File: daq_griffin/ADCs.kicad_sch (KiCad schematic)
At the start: 12 parts, among them J13 SENSOR, U13 ADS8866

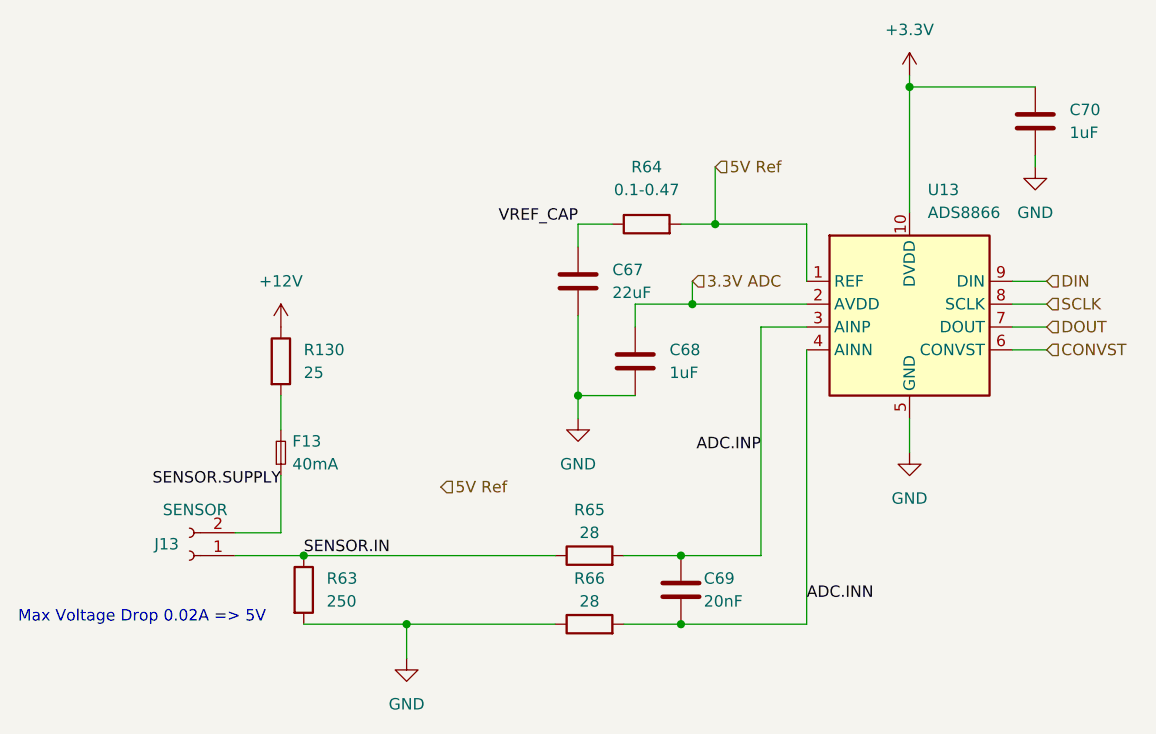
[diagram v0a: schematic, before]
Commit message: Add thermocouple connectors and minor layout changes.
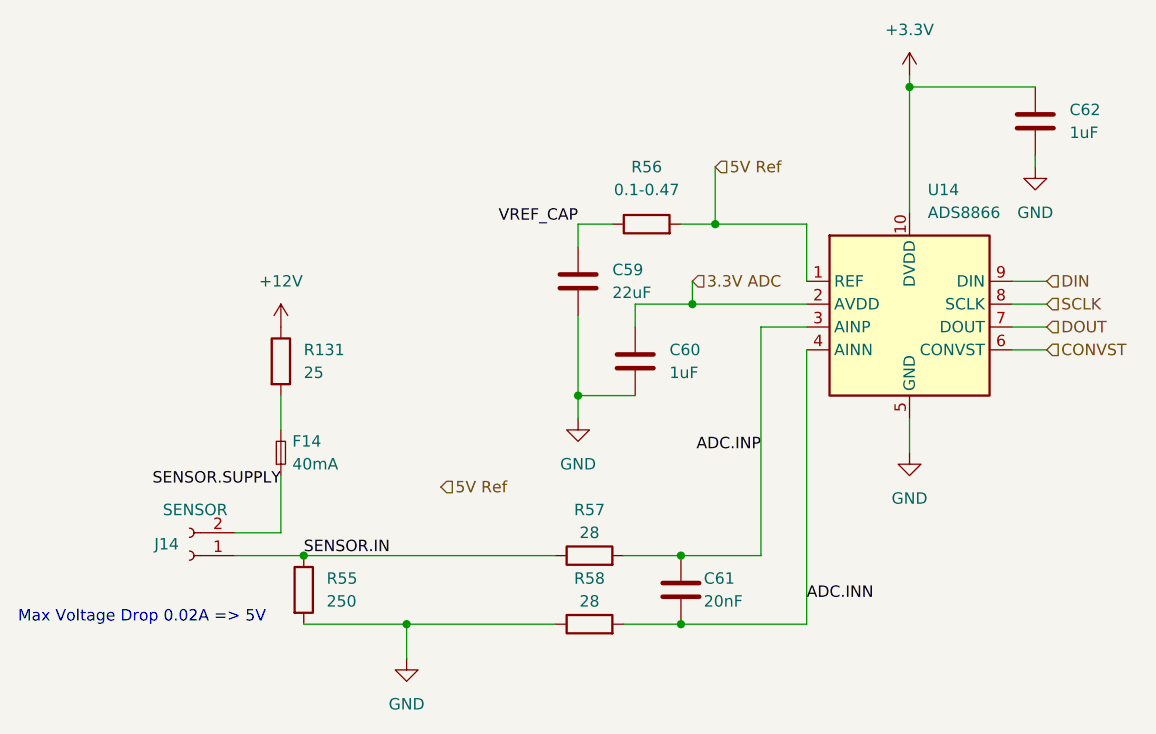
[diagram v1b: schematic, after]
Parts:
- renumbered C67 to C59, C68 to C60, C69 to C61, C70 to C62, F13 to F14, J13 to J14, R130 to R131, R63 to R55, R64 to R56, R65 to R57, R66 to R58, U13 to U14
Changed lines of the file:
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@@
 		(on_board yes)
 		(dnp no)
-		(property "Reference" "R65"
+		(property "Reference" "R57"
 			(at 109.22 97.79 90)
 			(effects
@@
 		(dnp no)
 		(fields_autoplaced yes)
-		(property "Reference" "#PWR0238"
+		(property "Reference" "#PWR0222"
 			(at 144.78 97.79 0)
 			(effects
@@
 		(dnp no)
 		(fields_autoplaced yes)
-		(property "Reference" "C70"
+		(property "Reference" "C62"
 			(at 162.56 53.3399 0)
 			(effects
@@
 		(dnp no)
 		(fields_autoplaced yes)
-		(property "Reference" "U13"
+		(property "Reference" "U14"
 			(at 146.7994 62.23 0)
 			(effects
@@
 		(dnp no)
 		(fields_autoplaced yes)
-		(property "Reference" "#PWR0235"
+		(property "Reference" "#PWR0219"
 			(at 144.78 53.34 0)
 			(effects
@@
 		(dnp no)
 		(fields_autoplaced yes)
-		(property "Reference" "C68"
+		(property "Reference" "C60"
 			(at 118.11 80.0099 0)
 			(effects
@@
 		(dnp no)
 		(fields_autoplaced yes)
-		(property "Reference" "#PWR0239"
+		(property "Reference" "#PWR0223"
 			(at 88.9 120.65 0)
 			(effects
@@
 		(on_board yes)
 		(dnp no)
-		(property "Reference" "J13"
+		(property "Reference" "J14"
 			(at 62.23 101.6 0)
 			(effects
@@
 		(on_board yes)
 		(dnp no)
-		(property "Reference" "C69"
+		(property "Reference" "C61"
 			(at 121.92 105.41 0)
 			(effects
@@
 		(dnp no)
 		(fields_autoplaced yes)
-		(property "Reference" "R63"
+		(property "Reference" "R55"
 			(at 80.01 105.4099 0)
 			(effects
@@
 		(dnp no)
 		(fields_autoplaced yes)
-		(property "Reference" "#PWR0241"
+		(property "Reference" "#PWR0225"
 			(at 74.93 81.28 0)
 			(effects
@@
 		(dnp no)
 		(fields_autoplaced yes)
-		(property "Reference" "#PWR0234"
+		(property "Reference" "#PWR0218"
 			(at 158.75 66.04 0)
 			(effects
@@
 		(dnp no)
 		(fields_autoplaced yes)
-		(property "Reference" "R64"
+		(property "Reference" "R56"
 			(at 115.57 59.69 90)
 			(effects
@@
 		(dnp no)
 		(fields_autoplaced yes)
-		(property "Reference" "#PWR0240"
+		(property "Reference" "#PWR0224"
 			(at 107.95 93.98 0)
 			(effects
@@
 		(dnp no)
 		(fields_autoplaced yes)
-		(property "Reference" "C67"
+		(property "Reference" "C59"
 			(at 111.76 71.1199 0)
 			(effects
@@
 		(on_board yes)
 		(dnp no)
-		(property "Reference" "R66"
+		(property "Reference" "R58"
 			(at 109.22 105.41 90)
 			(effects
@@
 		(dnp no)
 		(fields_autoplaced yes)
-		(property "Reference" "F13"
+		(property "Reference" "F14"
 			(at 76.2 90.1699 90)
 			(effects
@@
 		(dnp no)
 		(fields_autoplaced yes)
-		(property "Reference" "R130"
+		(property "Reference" "R131"
 			(at 77.47 80.0099 0)
 			(effects

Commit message: Rewired right side and fixed dual transistor
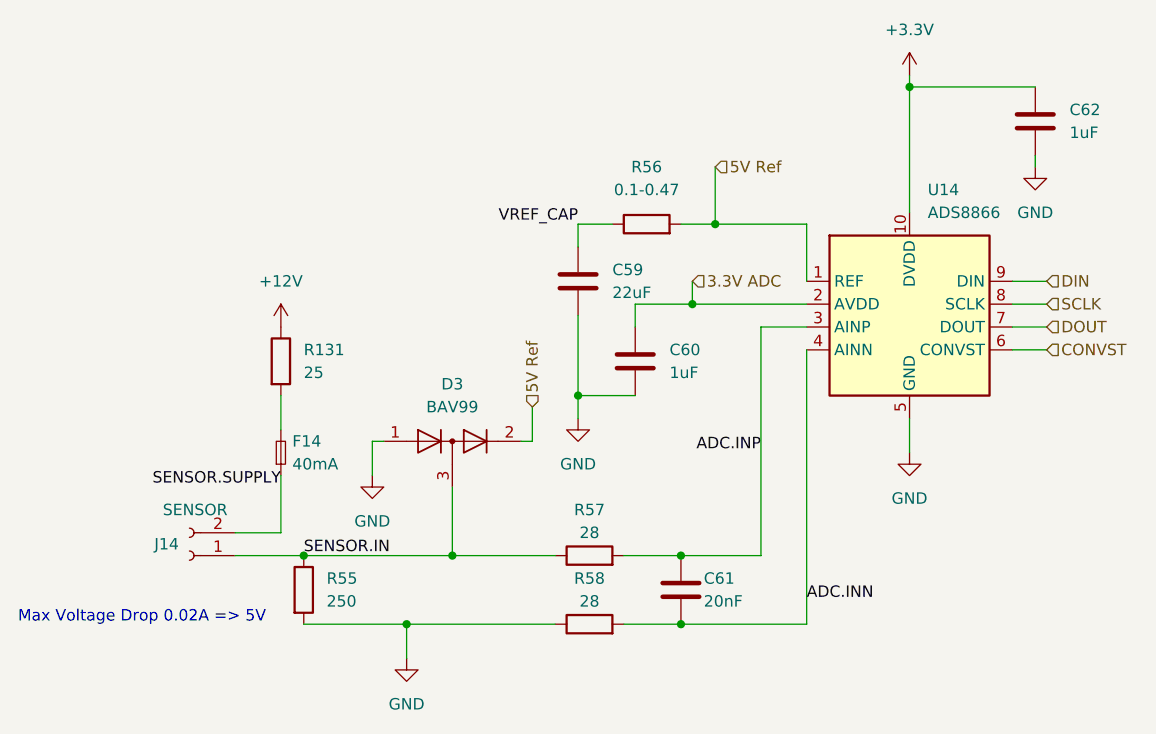
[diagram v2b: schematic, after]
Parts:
- added D3: BAV99, Package_TO_SOT_SMD:SOT-323_SC-70, symbol Diode:BAV99
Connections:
- net 5V Ref: now also D3.2 (A)
- net GND: now also D3.1 (K)
- net SENSOR.IN: now also D3.3 (K)

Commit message: Complete Silkscreen
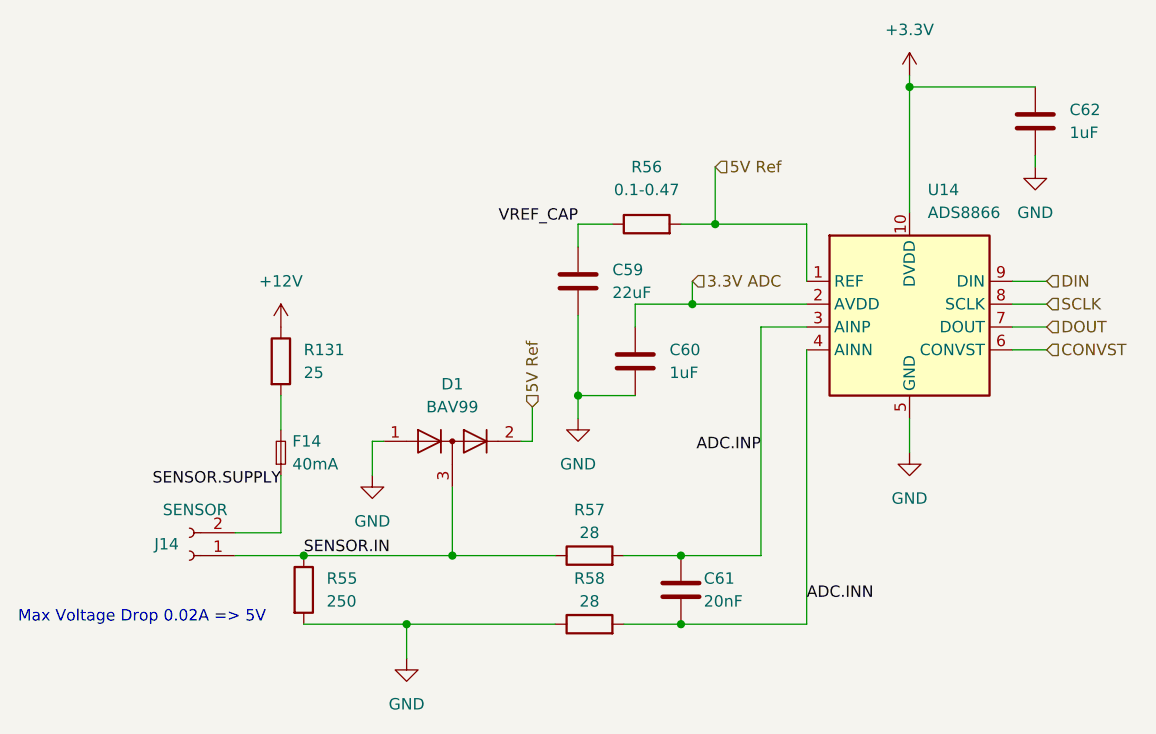
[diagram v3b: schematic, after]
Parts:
- renumbered D3 to D1
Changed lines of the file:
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@@
 		(dnp no)
 		(fields_autoplaced yes)
-		(property "Reference" "D3"
+		(property "Reference" "D1"
 			(at 93.98 83.82 0)
 			(effects

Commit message: Inductor footprint changed, ADC fuse value now 30mA, ADC 25R resistor now 22R, 0.1-0.47R resistor set to 0.47R
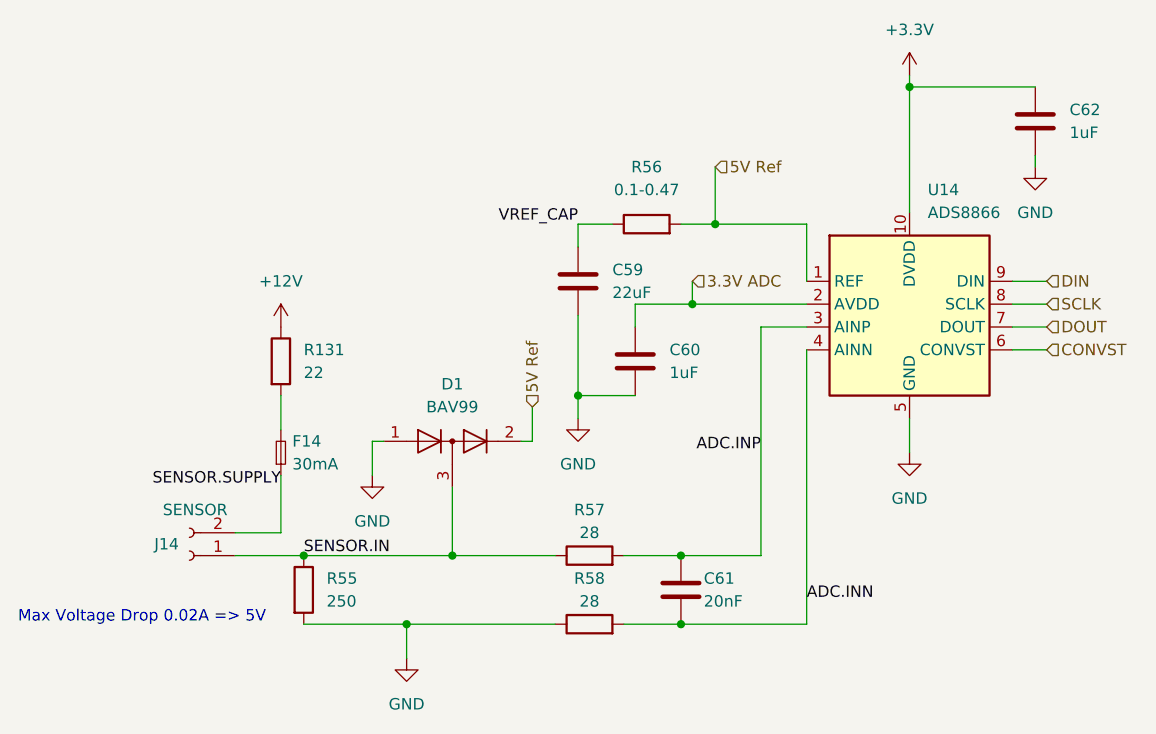
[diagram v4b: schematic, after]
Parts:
- F14: value 40mA -> 30mA
- R131: value 25 -> 22
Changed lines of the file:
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@@
 			)
 		)
-		(property "Value" "40mA"
+		(property "Value" "30mA"
 			(at 76.2 92.7099 90)
 			(effects
@@
 			)
 		)
-		(property "Value" "25"
+		(property "Value" "22"
 			(at 77.47 82.5499 0)
 			(effects

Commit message: Added JLCPCB part numbers to all back side components to be in PCBA
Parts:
- C59: LCSC (none) -> C5674
- C60, C62: LCSC (none) -> C1592
- C61: LCSC (none) -> C307483
- F14: LCSC (none) -> C914090
- R131: LCSC (none) -> C1203
- R55: LCSC (none) -> C2828898
- R56: LCSC (none) -> C175686
- R57, R58: LCSC (none) -> C217932
- U14: LCSC (none) -> C455432
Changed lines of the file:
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@@
+			)
+		)
+		(property "LCSC" "C217932"
+			(at 109.22 102.87 90)
+			(effects
+				(font
+					(size 1.27 1.27)
+				)
+				(hide yes)
 			)
 		)
@@
 			)
 		)
+		(property "LCSC" "C1592"
+			(at 158.75 54.61 0)
+			(effects
+				(font
+					(size 1.27 1.27)
+				)
+				(hide yes)
+			)
+		)
 		(pin "1"
 		)
@@
 			)
 		)
+		(property "LCSC" "C455432"
+			(at 144.78 76.2 0)
+			(effects
+				(font
+					(size 1.27 1.27)
+				)
+				(hide yes)
+			)
+		)
 		(pin "1"
 		)
@@
 		)
 		(property "Description" ""
+			(at 114.3 81.28 0)
+			(effects
+				(font
+					(size 1.27 1.27)
+				)
+				(hide yes)
+			)
+		)
+		(property "LCSC" "C1592"
 			(at 114.3 81.28 0)
 			(effects
@@
 			)
 		)
+		(property "LCSC" "C307483"
+			(at 119.38 106.68 0)
+			(effects
+				(font
+					(size 1.27 1.27)
+				)
+				(hide yes)
+			)
+		)
 		(pin "1"
 		)
@@
 		)
 		(property "Description" ""
+			(at 77.47 106.68 0)
+			(effects
+				(font
+					(size 1.27 1.27)
+				)
+				(hide yes)
+			)
+		)
+		(property "LCSC" "C2828898"
 			(at 77.47 106.68 0)
 			(effects
@@
 			)
 		)
+		(property "LCSC" "C175686"
+			(at 115.57 66.04 90)
+			(effects
+				(font
+					(size 1.27 1.27)
+				)
+				(hide yes)
+			)
+		)
 		(pin "1"
 		)
@@
 			)
 		)
+		(property "LCSC" "C5674"
+			(at 107.95 72.39 0)
+			(effects
+				(font
+					(size 1.27 1.27)
+				)
+				(hide yes)
+			)
+		)
 		(pin "1"
 		)
@@
 		(property "Description" ""
 			(at 109.22 110.49 0)
+			(effects
+				(font
+					(size 1.27 1.27)
+				)
+				(hide yes)
+			)
+		)
+		(property "LCSC" "C217932"
+			(at 109.22 110.49 90)
 			(effects
 				(font
@@
 			)
 		)
+		(property "LCSC" "C914090"
+			(at 74.93 91.44 90)
+			(effects
+				(font
+					(size 1.27 1.27)
+				)
+				(hide yes)
+			)
+		)
 		(pin "1"
 		)
@@
 			(at 74.93 81.28 0)
 			(effects
+				(font
+					(size 1.27 1.27)
+				)
+				(hide yes)
+			)
+		)
+		(property "LCSC" "C1203"
+			(at 74.93 81.28 0)
+			(effects
